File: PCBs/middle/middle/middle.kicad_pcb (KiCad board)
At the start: 4 copper layers, 95.1 x 95.1 mm, 27 parts, among them J15 Screw_Terminal_01x02, J16 Screw_Terminal_01x02, J17 Screw_Terminal_01x02, J18 Screw_Terminal_01x02, J19 Screw_Terminal_01x02, J2 Screw_Terminal_01x03, J21 Screw_Terminal_01x02, J3 Screw_Terminal_01x03, J4 Screw_Terminal_01x03, J5 Screw_Terminal_01x03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

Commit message: nrf middle update 1 (NOT DONE)
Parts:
- added C1: 100u, Capacitor_THT:CP_Radial_D6.3mm_P2.50mm, F.Cu at (184.2, 58.4)
- U3: value RFM69HCW -> NRF24L01_Breakout; footprint RF_Module:HOPERF_RFM9XW_THT -> RF_Module:nRF24L01_Breakout
- moved U3 7.89 mm to (190.1, 56.6)
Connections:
- U1 pad 34: /RFMreset -> /IRQ
- U1 pad 35: /RFM0 -> /CE
- U3 pad 2: /MISO -> +3.3V
- U3 pad 3: /MOSI -> /IRQ
- U3 pad 4: /SCLK -> /NSS
- U3 pad 5: /NSS -> /SCLK
- U3 pad 6: /RFMreset -> /MOSI
- U3 pad 7: unconnected-(U3-DIO5-Pad7) -> /MISO
- U3 pad 8: GND -> /CE
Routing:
- net /RFM0: track 120.7 -> 0.00 mm
- net /CE: track 0.00 -> 113.2 mm
- net /IRQ: track 0.00 -> 99.5 mm
- net /RFMreset: track 95.5 -> 0.00 mm
- net +3.3V: track 200.5 -> 224.7 mm
- net /NSS: track 83.5 -> 105.1 mm
- net /MISO: track 73.9 -> 66.3 mm, vias 1 -> 0
- net /SCLK: track 70.0 -> 73.6 mm
- net /MOSI: track 66.9 -> 68.7 mm

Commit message: FINAL?
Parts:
- F1: footprint Fuse:Fuseholder_Clip-5x20mm_Schurter_OG_Lateral_P15.00x5.00mm_D1.3mm_Horizontal -> Fuse:Fuseholder_Clip-5x20mm_Littelfuse_520_Inline_P20.50x5.80mm_D1.30mm_Horizontal
- R1, R2: footprint Resistor_THT:R_Axial_DIN0204_L3.6mm_D1.6mm_P5.08mm_Horizontal -> Resistor_THT:R_Axial_DIN0207_L6.3mm_D2.5mm_P10.16mm_Horizontal
- moved R1 18.4 mm to (180.0, 65.6), turned to -90 degrees
- moved R2 7.04 mm to (176.8, 65.6)
- moved F1 3.17 mm to (136.2, 125.2)
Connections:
- U1 pad 34: /IRQ -> /CE
- U1 pad 35: /CE -> /IRQ
- U3 pad 3: /IRQ -> /CE
- U3 pad 8: /CE -> /IRQ
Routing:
- net /Vbat: track 86.2 -> 55.3 mm
- net VCC: track 6.42 -> 21.9 mm
- net /IRQ: track 99.5 -> 113.2 mm
- net /CE: track 113.2 -> 99.5 mm
- net Net-(J18-Pin_1): track 17.0 -> 15.3 mm
- net /M2B: track 54.7 -> 56.2 mm
- net /M2A: track 56.0 -> 57.6 mm
- net /M3A: track 53.6 -> 55.0 mm
- net +5V: track 5.00 -> 5.80 mm
- net /M4B: track 56.1 -> 55.5 mm

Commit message: final
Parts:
- added J1: Conn_01x04_Pin, Connector_PinSocket_2.54mm:PinSocket_1x04_P2.54mm_Vertical, F.Cu at (167.9, 122.4)
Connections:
- U1 pad 24: unconnected-(U1-A10-Pad24) -> Net-(J1-Pin_3)
- U1 pad 25: unconnected-(U1-A11-Pad25) -> Net-(J1-Pin_4)
- U2 pad JP2_2: unconnected-(U2-P0-PadJP2_2) -> (no net)
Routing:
- net /IRQ: track 113.2 -> 107.2 mm
- net Net-(J1-Pin_4): track 0.00 -> 5.71 mm
- net Net-(J1-Pin_3): track 0.00 -> 5.71 mm
- net +3.3V: track 224.7 -> 229.2 mm
- net GND: vias 40 -> 42
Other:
- board text added: "5Vin"
- board text added: "M1B M1A"
- board text added: "M3A M2A M2B"
- board text added: "M4B M4A M3B"
- board text removed: "GND 5Vin"
- board text removed: "M1"
- board text removed: "M2"
- board text removed: "M3"
- board text removed: "M4"

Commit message: pcb final final final?
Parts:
- U1 Teensy 4.1: renamed from U1
- U2 BNO08x: renamed from U2
- U3 nRF24L01: renamed from U3
- moved J1 1.14 mm to (167.1, 123.2)
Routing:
- net +3.3V: track 229.2 -> 232.1 mm
- net Net-(J1-Pin_4): track 5.71 -> 6.86 mm
- net Net-(J1-Pin_3): track 5.71 -> 6.86 mm
- net /SCLK: track 73.7 -> 74.4 mm
- net GND: vias 42 -> 41
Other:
- board text added: "2/6/2026 MINDSTORMERS main board designed by aiden"
- board text added: "SDA SCL GND 3.3V"

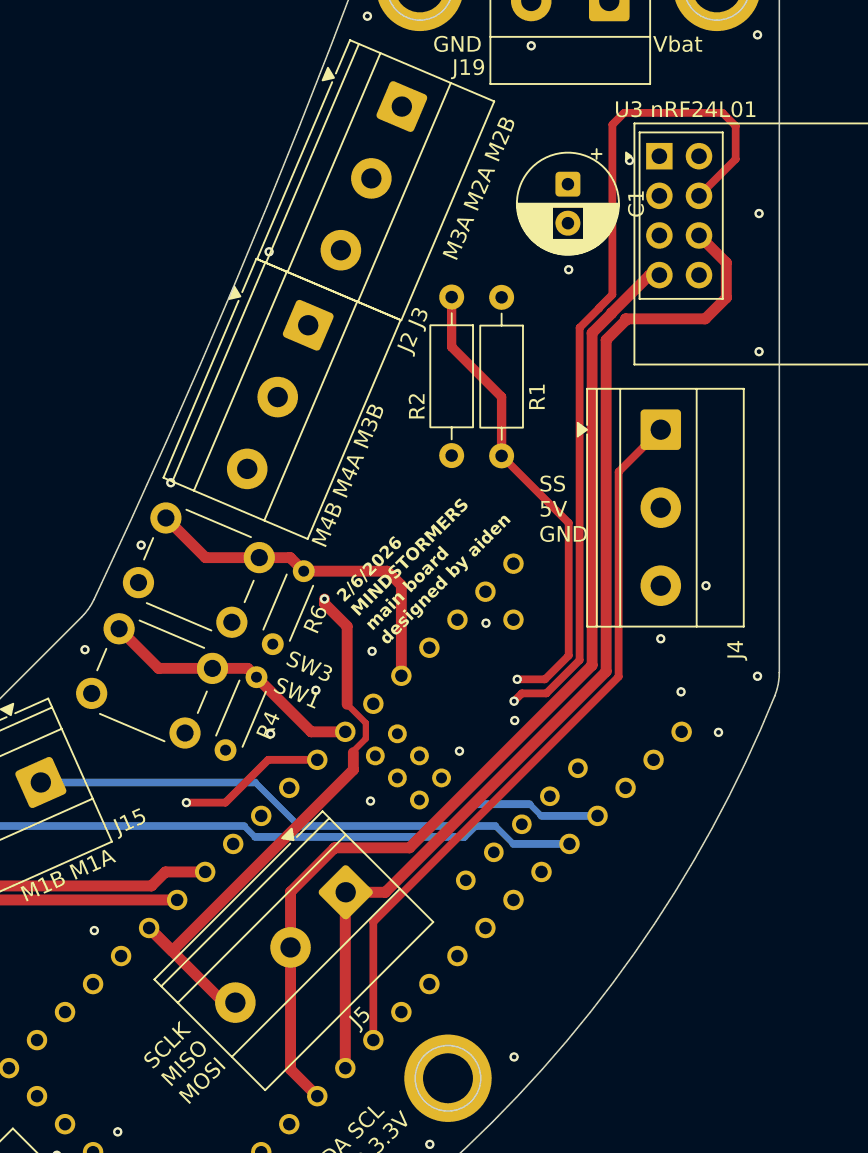
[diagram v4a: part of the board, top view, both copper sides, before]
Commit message: final v4 add esc to middle
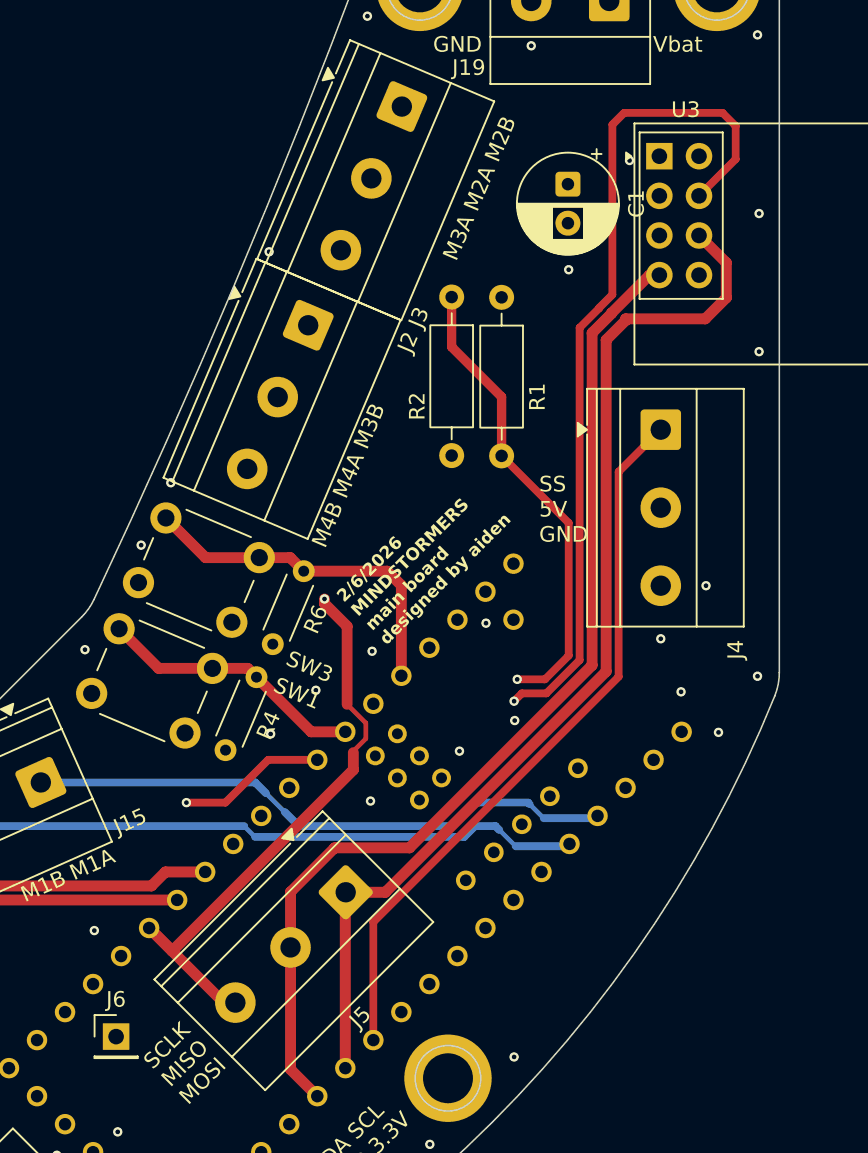
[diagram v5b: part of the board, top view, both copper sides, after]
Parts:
- added J6: Conn_01x01_Pin, Connector_PinHeader_2.54mm:PinHeader_1x01_P2.54mm_Vertical, F.Cu at (155.3, 113.0)
- U1: renamed from U1 Teensy 4.1
- U2: renamed from U2 BNO08x
- U3: renamed from U3 nRF24L01
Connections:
- U1 pad 37: unconnected-(U1-CS3-Pad37) -> Net-(J6-Pin_1)
- U2 pad JP2_2: (no net) -> unconnected-(U2-P0-PadJP2_2)
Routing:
- net Net-(J6-Pin_1): track 0.00 -> 13.3 mm
